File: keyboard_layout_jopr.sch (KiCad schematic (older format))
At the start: 229 parts, among them SW1 SW_Push, U1 ATmega32U4-AU, U2 SOT65P210X110, Y1 16MHz

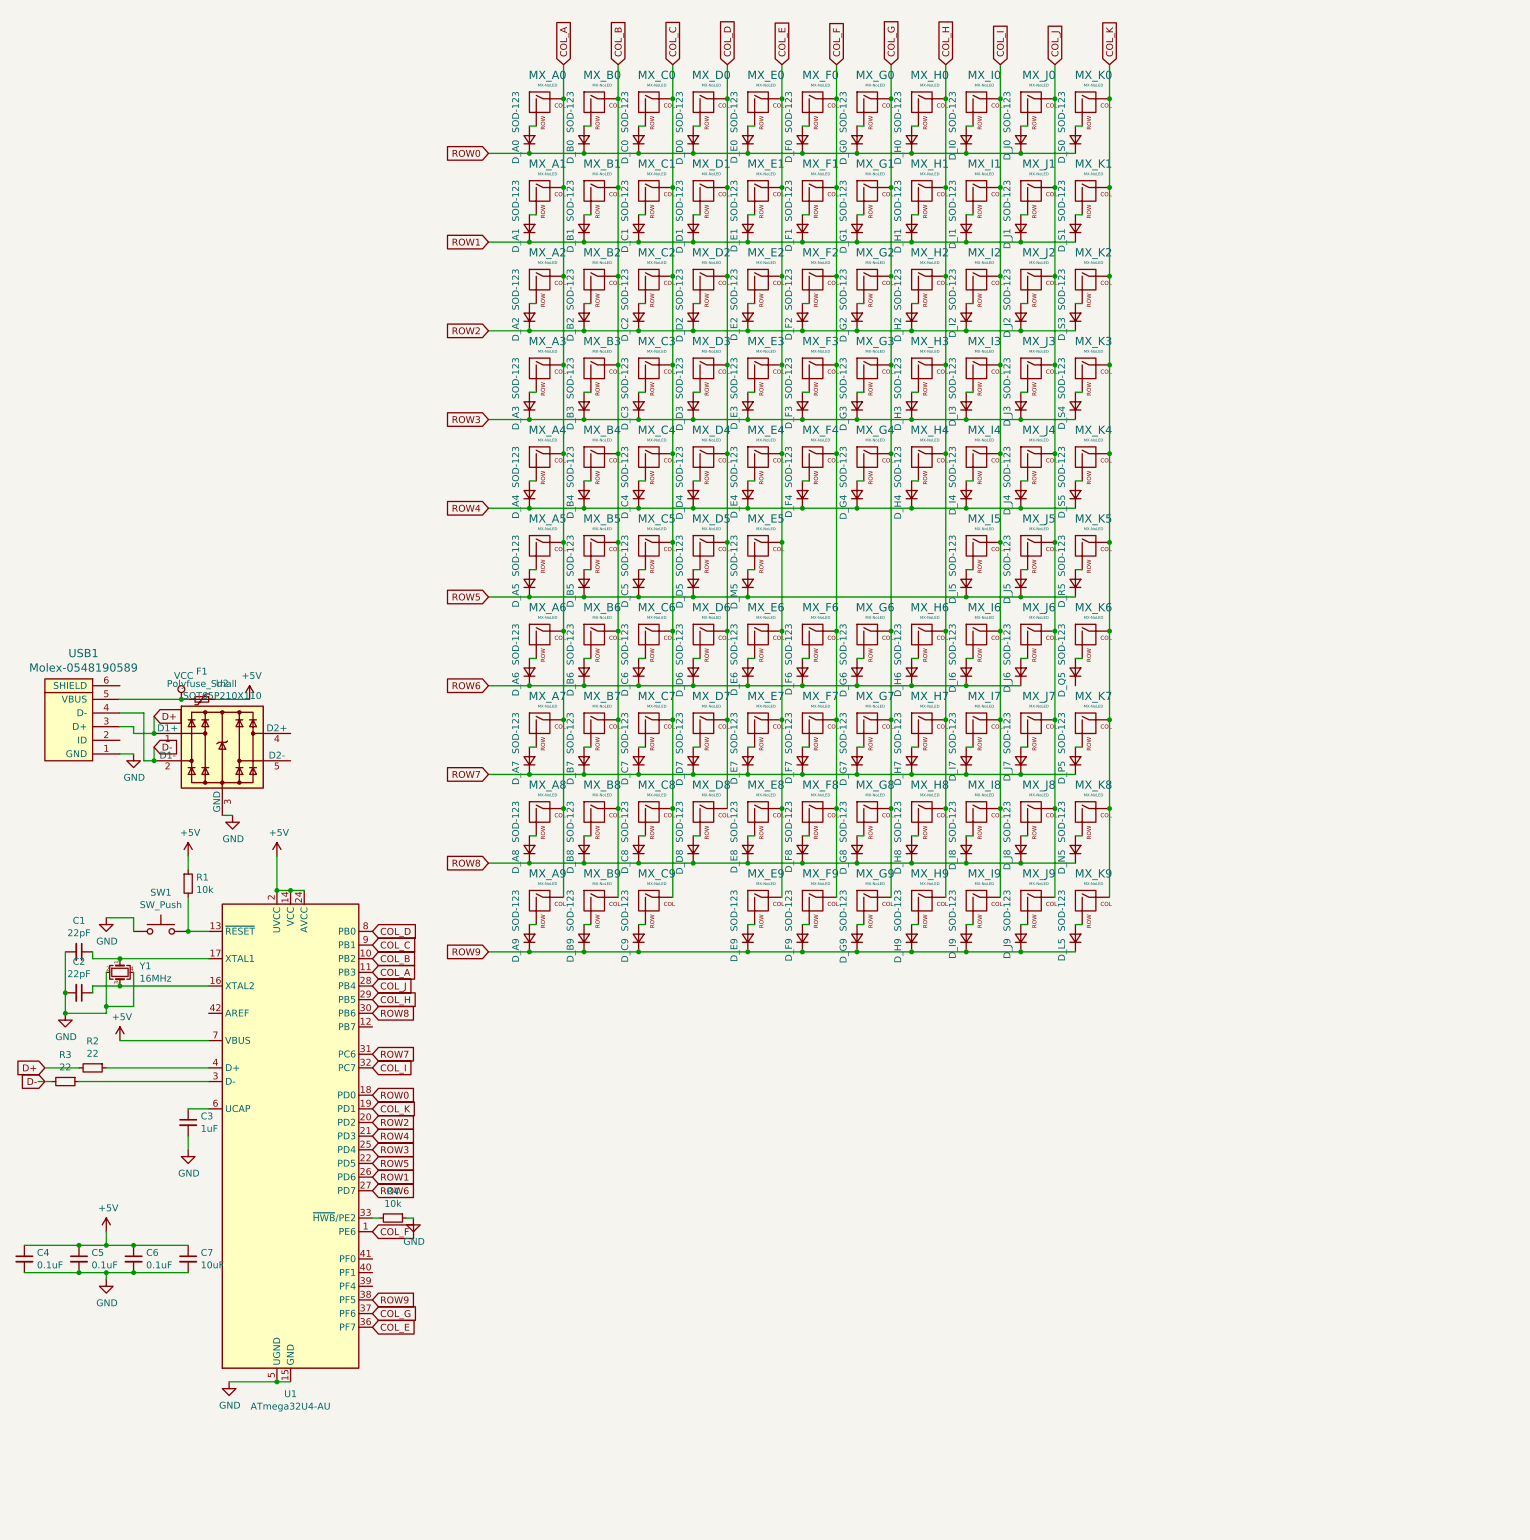
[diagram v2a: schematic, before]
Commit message: added LEDs for Lock keys
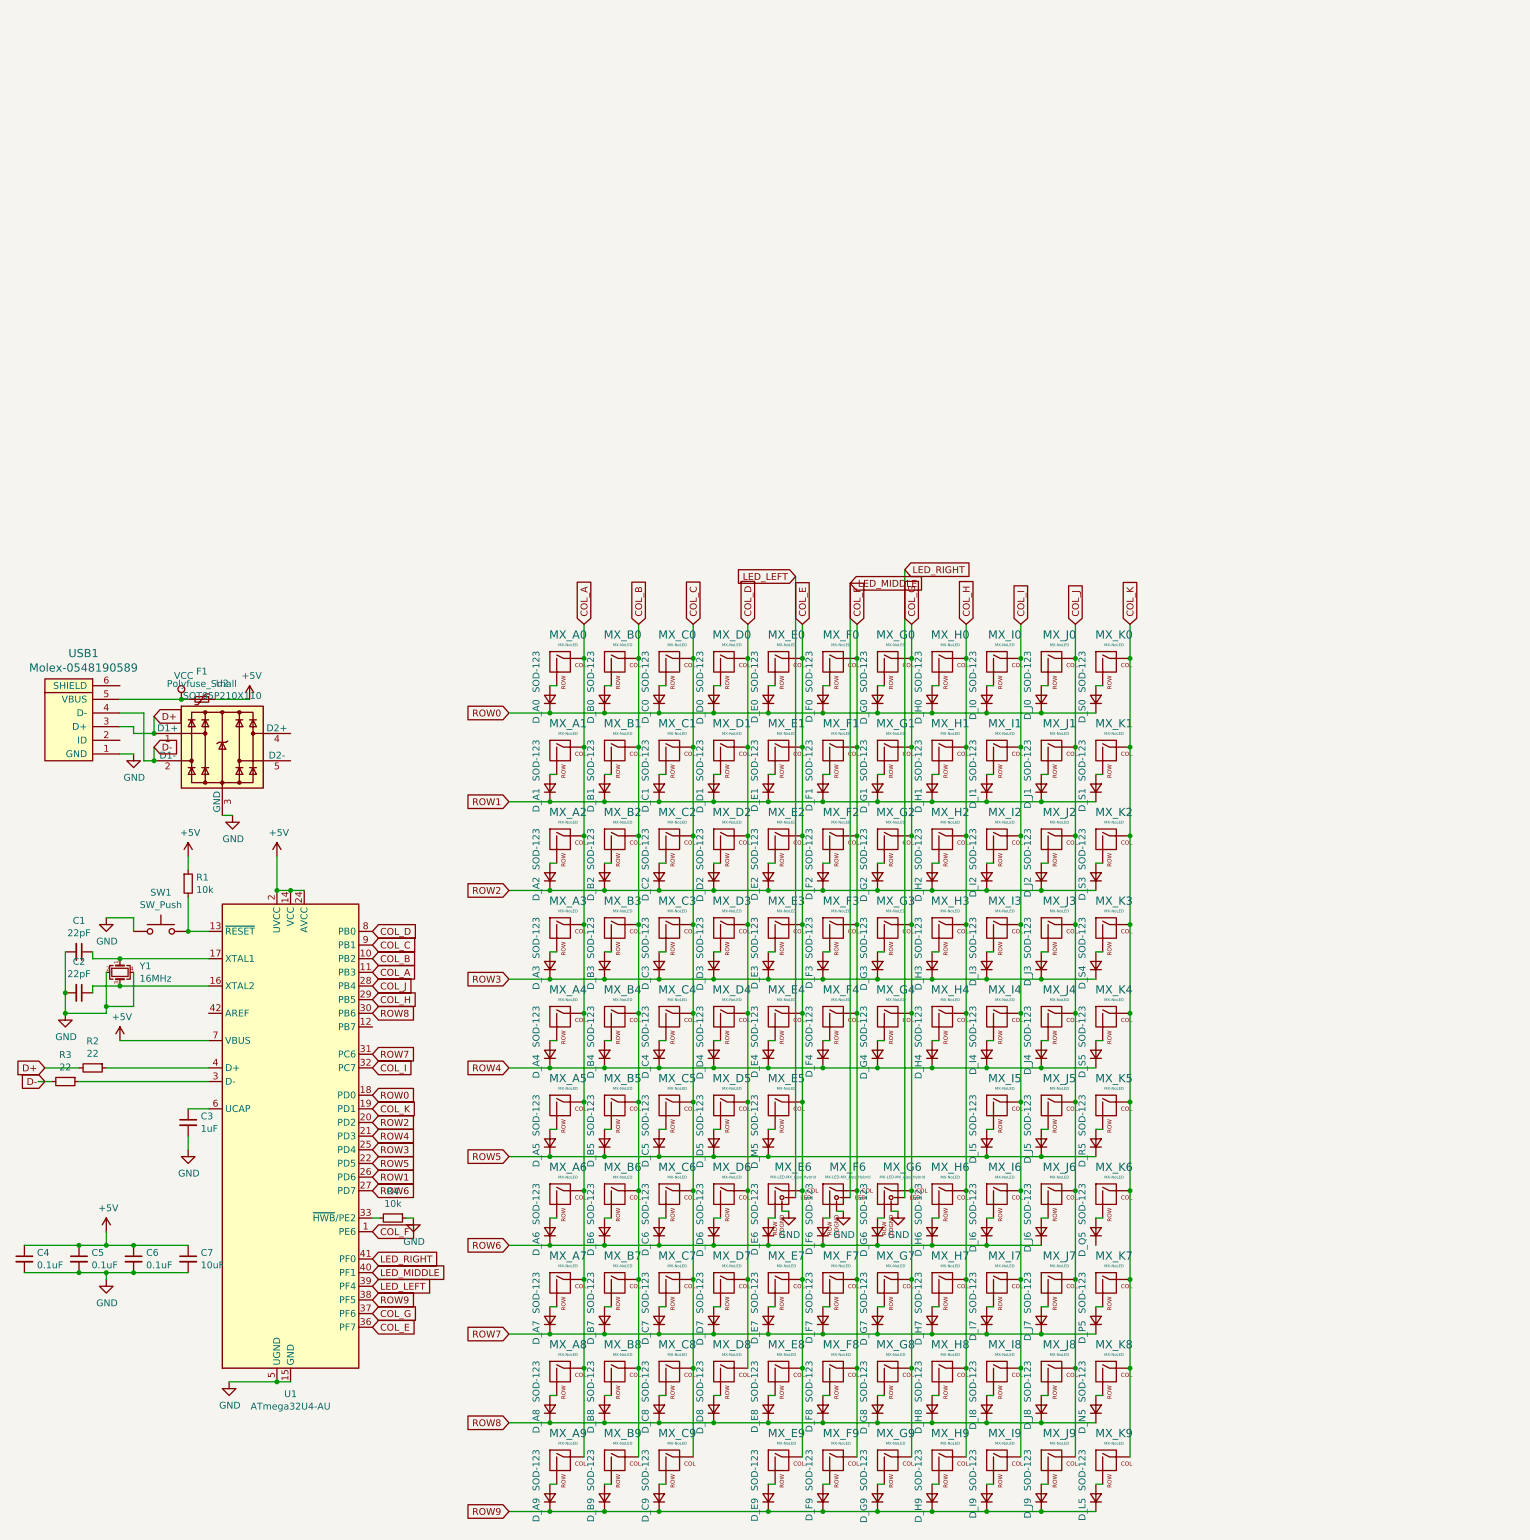
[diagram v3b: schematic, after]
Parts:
- removed MX_E6, MX_F6, MX_G6: MX-NoLED, MX_Only:MXOnly-1U-NoLED, symbol keyboard_layout_jopr-rescue:MX-NoLED-MX_Alps_Hybrid
- added MX_E6, MX_F6, MX_G6: MX-LED-MX_Alps_Hybrid, MX_Only:MXOnly-1U-FLIPPED, symbol keyboard_layout_jopr-rescue:MX-LED-MX_Alps_Hybrid
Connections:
- net COL_E: now also MX_E6.1 (COL)
- net COL_F: now also MX_F6.1 (COL)
- net COL_G: now also MX_G6.1 (COL)
- net GND: now also MX_E6.4 (LEDGND), MX_F6.4 (LEDGND), MX_G6.4 (LEDGND)
- net LED_LEFT: now reaches U1.39 (PF4)
- net LED_LEFT: now also MX_E6.3 (LED)
- net LED_MIDDLE: now reaches U1.40 (PF1)
- net LED_MIDDLE: now also MX_F6.3 (LED)
- net LED_RIGHT: now reaches U1.41 (PF0)
- net LED_RIGHT: now also MX_G6.3 (LED)
- net at D_E6.2 (A): now also MX_E6.2 (ROW)
- net at D_F6.2 (A): now also MX_F6.2 (ROW)
- net at D_G6.2 (A): now also MX_G6.2 (ROW)
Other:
- moved on the sheet: D_A0, D_A1, D_A2, D_A3, D_A4, D_A5, D_A6, D_A7, D_A8, D_A9, D_B0, D_B1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

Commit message: removed NumLock
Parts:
- removed MX_E6: MX-LED-MX_Alps_Hybrid, MX_Only:MXOnly-1U-FLIPPED, symbol keyboard_layout_jopr-rescue:MX-LED-MX_Alps_Hybrid
- added MX_E6: MX-NoLED, MX_Only:MXOnly-1U-NoLED, symbol keyboard_layout_jopr-rescue:MX-NoLED-MX_Alps_Hybrid
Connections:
- net COL_E: now also MX_E6.1 (COL)
- net at D_E6.2 (A): now also MX_E6.2 (ROW)
- net LED_LEFT: no longer names the net of U1.39 (PF4)
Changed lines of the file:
@@
 Connection ~ 1550 1450
-Wire Wire Line
-	6300 3950 6300 4600
 Wire Wire Line
 	6700 3300 6700 4600
 Wire Wire Line
 	7100 3300 7100 4600
-$Comp
-L keyboard_layout_jopr-rescue:MX-LED-MX_Alps_Hybrid MX_E6
-U 1 1 5D1102C1
-P 6150 4650
-F 0 "MX_E6" H 6232 4874 60  0000 C CNN
-F 1 "MX-LED-MX_Alps_Hybrid" H 6232 4800 20  0000 C CNN
-F 2 "MX_Only:MXOnly-1U-FLIPPED" H 5525 4625 60  0001 C CNN
-F 3 "" H 5525 4625 60  0001 C CNN
-	1    6150 4650
-	1    0    0    -1
-$EndComp
-Connection ~ 6300 4600
-Wire Wire Line
-	6300 4600 6300 5250
 $Comp
 L keyboard_layout_jopr-rescue:MX-LED-MX_Alps_Hybrid MX_F6
@@
 	1    0    0    -1
 $EndComp
-$Comp
-L power:GND #PWR0104
-U 1 1 5D11AF82
-P 6200 4750
-F 0 "#PWR0104" H 6200 4500 50  0001 C CNN
-F 1 "GND" H 6205 4577 50  0000 C CNN
-F 2 "" H 6200 4750 50  0001 C CNN
-F 3 "" H 6200 4750 50  0001 C CNN
-	1    6200 4750
-	1    0    0    -1
-$EndComp
-Wire Wire Line
-	6150 4750 6200 4750
 Wire Wire Line
 	6550 4750 6600 4750
 Wire Wire Line
 	6950 4750 7000 4750
-Wire Wire Line
-	6250 4650 6250 100
-Text GLabel 6250 100  0    50   Input ~ 0
-LED_LEFT
 Wire Wire Line
 	6650 4650 6650 150
@@
 Text GLabel 7050 50   2    50   Input ~ 0
 LED_RIGHT
-Text GLabel 3150 5300 2    50   Input ~ 0
-LED_LEFT
 Text GLabel 3150 5200 2    50   Input ~ 0
 LED_MIDDLE
 Text GLabel 3150 5100 2    50   Input ~ 0
 LED_RIGHT
+Wire Wire Line
+	6300 3950 6300 4600
+$Comp
+L keyboard_layout_jopr-rescue:MX-NoLED-MX_Alps_Hybrid MX_E6
+U 1 1 5D2D876E
+P 6150 4650
+F 0 "MX_E6" H 6183 4873 60  0000 C CNN
+F 1 "MX-NoLED" H 6183 4799 20  0000 C CNN
+F 2 "MX_Only:MXOnly-1U-NoLED" H 5525 4625 60  0001 C CNN
+F 3 "" H 5525 4625 60  0001 C CNN
+	1    6150 4650
+	1    0    0    -1
+$EndComp
+Connection ~ 6300 4600
+Wire Wire Line
+	6300 4600 6300 5250
 $EndSCHEMATC
